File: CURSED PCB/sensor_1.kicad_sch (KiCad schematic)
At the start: 9 parts, among them U1 OPA196xDBV

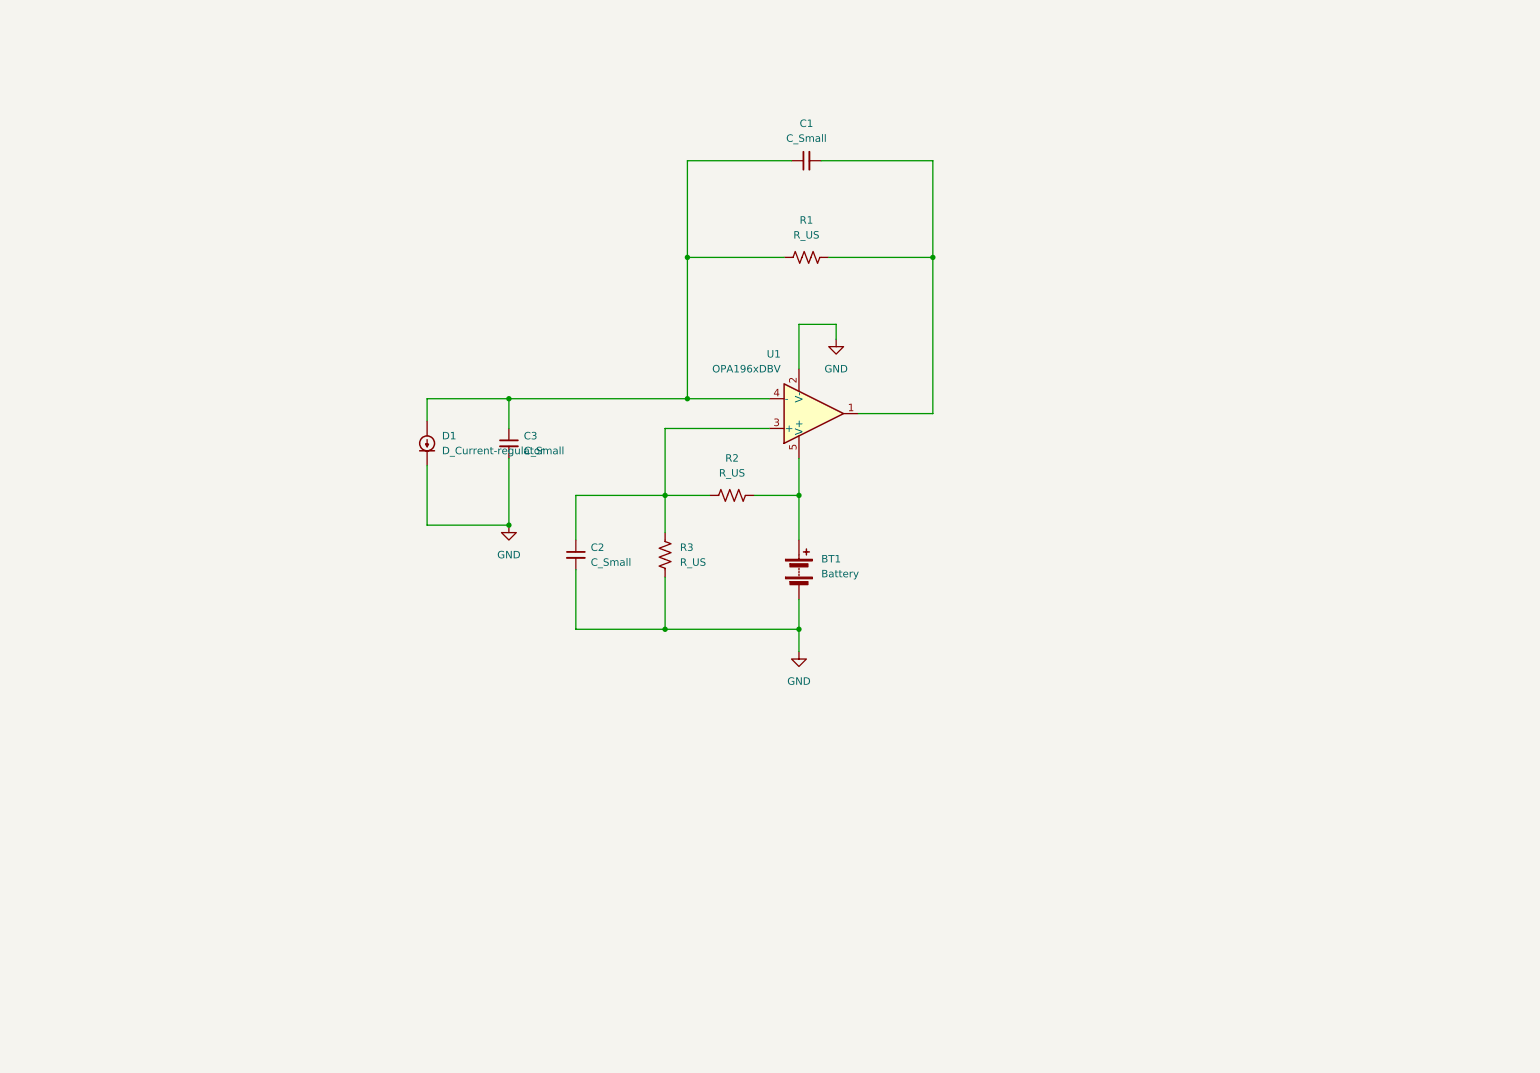
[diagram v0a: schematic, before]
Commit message: Updated PCB compoments
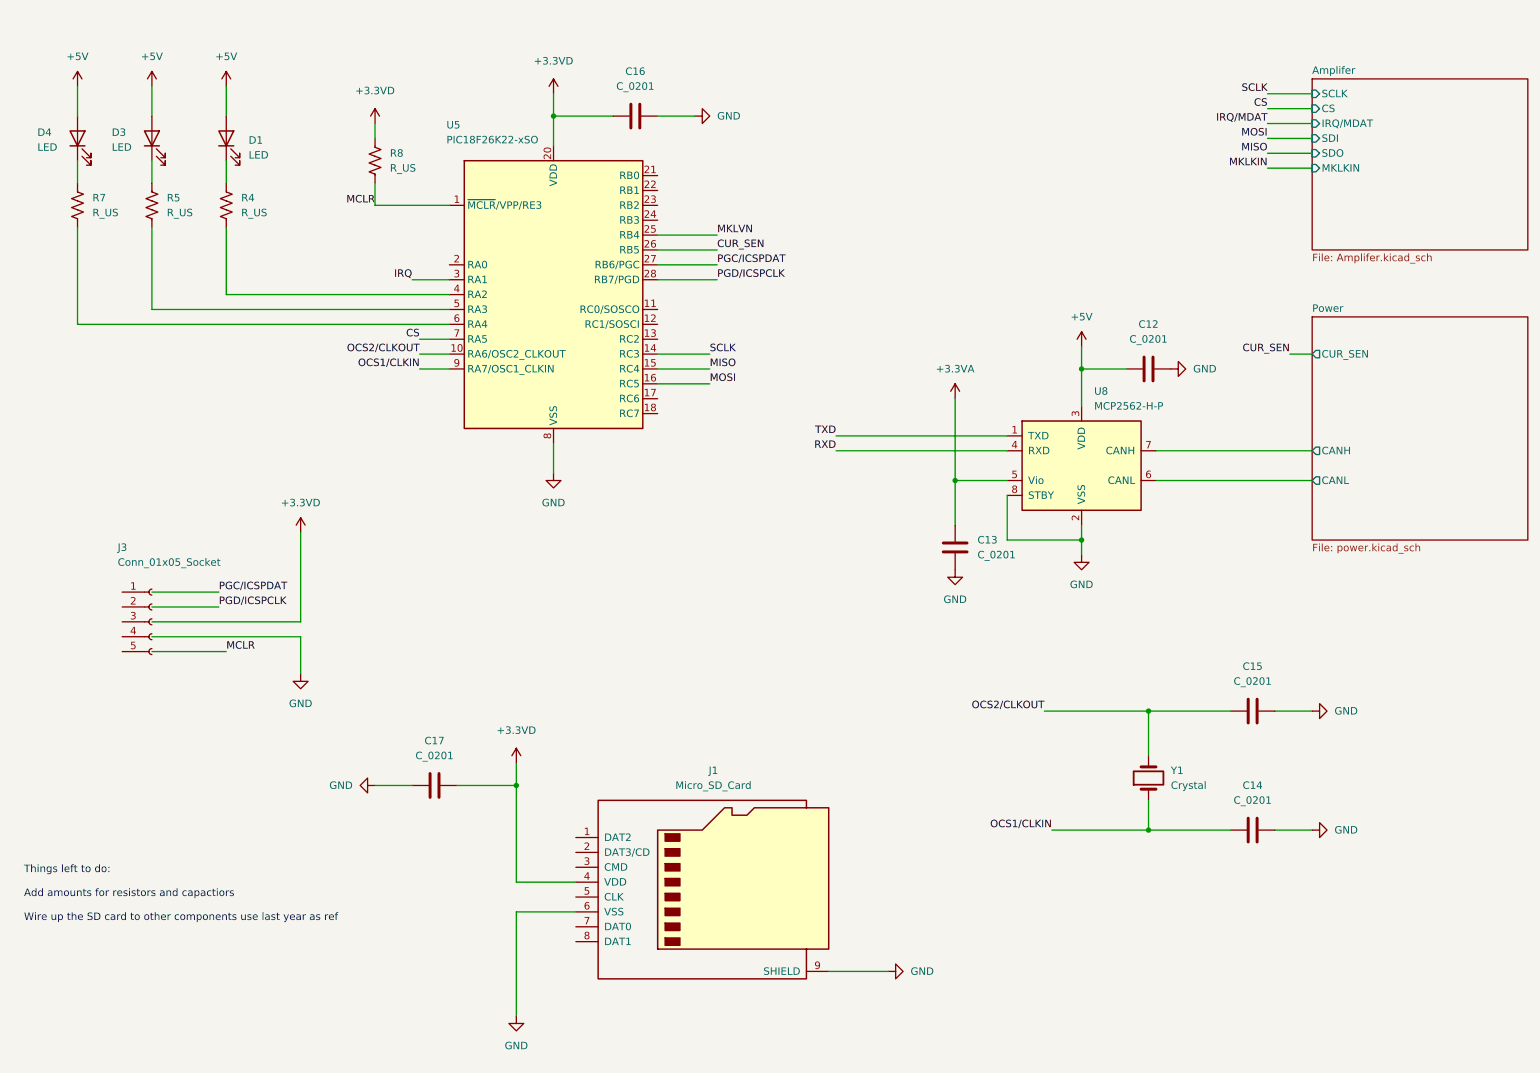
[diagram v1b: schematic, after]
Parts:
- removed BT1: Battery, symbol Device:Battery
- removed C1, C2, C3: C_Small, symbol Device:C_Small
- removed D1: D_Current-regulator, symbol Device:D_Current-regulator
- removed R1, R2, R3: R_US, symbol Device:R_US
- removed U1: OPA196xDBV, Package_TO_SOT_SMD:SOT-23-5, symbol Amplifier_Operational:OPA196xDBV
- added C12, C13, C14, C15, C16, C17: C_0201, PCM_Capacitor_SMD_AKL:C_0201_0603Metric, symbol PCM_Capacitor_US_AKL:C_0201
- added D1, D3, D4: LED, symbol Device:LED
- added J1: Micro_SD_Card, symbol Connector:Micro_SD_Card
- added J3: Conn_01x05_Socket, symbol Connector:Conn_01x05_Socket
- added R4, R5, R7, R8: R_US, symbol Device:R_US
- added U5: PIC18F26K22-xSO, Package_SO:SOIC-28W_7.5x17.9mm_P1.27mm, symbol MCU_Microchip_PIC18:PIC18F26K22-xSO
- added U8: MCP2562-H-P, Package_DIP:DIP-8_W7.62mm, symbol Interface_CAN_LIN:MCP2562-H-P
- added Y1: Crystal, symbol Device:Crystal
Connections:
- net GND: now also C12.2, C13.1, C14.2, C15.2, C16.2, C17.2, J1.6 (VSS), J1.9 (SHIELD), U5.19 (VSS), U5.8 (VSS), U8.2 (VSS), U8.8 (STBY)
- new net: R4.2, U5.4 (RA2)
- new net: R5.2, U5.5 (RA3)
- new net: R7.2, U5.6 (RA4)
- new net: D1.1 (K), R4.1
- new net: D4.1 (K), R7.1
- new net: D3.1 (K), R5.1
- new net +3.3VA: C13.2, U8.5 (Vio)
- new net +3.3VD: C16.1, C17.1, J1.4 (VDD), R8.1, U5.20 (VDD)
- new net +5V: C12.1, D1.2 (A), D3.2 (A), D4.2 (A), U8.3 (VDD)
- new net CS: U5.7 (RA5)
- new net CUR_SEN: U5.26 (RB5)
- new net IRQ: U5.3 (RA1)
- new net MCLR: R8.2, U5.1 (~{MCLR}/VPP/RE3)
- new net MISO: U5.15 (RC4)
- new net MKLVN: U5.25 (RB4)
- new net MOSI: U5.16 (RC5)
- new net OCS1/CLKIN: C14.1, U5.9 (RA7/OSC1_CLKIN), Y1.1
- new net OCS2/CLKOUT: C15.1, U5.10 (RA6/OSC2_CLKOUT), Y1.2
- new net PGC/ICSPDAT: U5.27 (RB6/PGC)
- new net PGD/ICSPCLK: U5.28 (RB7/PGD)
- new net Power/CANH: U8.7 (CANH)
- new net Power/CANL: U8.6 (CANL)
- new net RXD: U8.4 (RXD)
- new net SCLK: U5.14 (RC3)
- new net TXD: U8.1 (TXD)
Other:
- added sheet Amplifer (Amplifer.kicad_sch)
- added sheet Power (power.kicad_sch)
- note added: "Things left to do: Add amounts for resistors and capactiors Wire up the SD card to other components use last year as ref"

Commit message: Added some amplifer stuff
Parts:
- D1: value LED -> RED LED
- D2: renamed from D3; value LED -> BLUE LED
- D3: renamed from D4; value LED -> GREEN LED
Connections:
- net CS: now also J1.2 (DAT3/CD)
- net MISO: now also J1.7 (DAT0)
- net MOSI: now also J1.3 (CMD)
- net SCLK: now also J1.5 (CLK)
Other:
- note added: "Things left to do: Add amounts for resistors and capactiors, use last year as ref"
- note removed: "Things left to do: Add amounts for resistors and capactiors Wire up the SD card to other components use last year as ref"
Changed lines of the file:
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@@
 	(generator_version "9.0")
 	(paper "A4")
-	(text "Things left to do:\n\nAdd amounts for resistors and capactiors\n\nWire up the SD card to other components use last year as ref"
+	(text "Things left to do:\n\nAdd amounts for resistors and capactiors, use last year as ref\n"
 		(exclude_from_sim no)
-		(at 16.256 163.322 0)
+		(at 183.388 174.498 0)
 		(effects
 			(font
@@
 	(wire
 		(pts
+			(xy 63.5 163.83) (xy 110.49 163.83)
+		)
+		(stroke
+			(width 0)
+			(type default)
+		)
+	)
+	(wire
+		(pts
 			(xy 110.49 161.29) (xy 100.33 161.29)
 		)
@@
 	(wire
 		(pts
+			(xy 63.5 168.91) (xy 110.49 168.91)
+		)
+		(stroke
+			(width 0)
+			(type default)
+		)
+	)
+	(wire
+		(pts
 			(xy 196.85 100.33) (xy 196.85 102.87)
 		)
@@
 	(wire
 		(pts
+			(xy 64.77 156.21) (xy 110.49 156.21)
+		)
+		(stroke
+			(width 0)
+			(type default)
+		)
+	)
+	(wire
+		(pts
 			(xy 50.8 60.96) (xy 88.9 60.96)
 		)
@@
 		(pts
 			(xy 38.1 111.76) (xy 49.53 111.76)
+		)
+		(stroke
+			(width 0)
+			(type default)
+		)
+	)
+	(wire
+		(pts
+			(xy 64.77 158.75) (xy 110.49 158.75)
 		)
 		(stroke
@@
 		)
 	)
+	(label "SCLK"
+		(at 63.5 163.83 0)
+		(effects
+			(font
+				(size 1.27 1.27)
+			)
+			(justify left bottom)
+		)
+	)
 	(label "MCLR"
 		(at 76.2 45.72 180)
@@
 		)
 	)
+	(label "MISO"
+		(at 63.5 168.91 0)
+		(effects
+			(font
+				(size 1.27 1.27)
+			)
+			(justify left bottom)
+		)
+	)
 	(label "CS"
 		(at 83.82 68.58 180)
@@
 		)
 	)
+	(label "CS"
+		(at 64.77 156.21 0)
+		(effects
+			(font
+				(size 1.27 1.27)
+			)
+			(justify left bottom)
+		)
+	)
 	(label "OCS2{slash}CLKOUT"
 		(at 190.5 132.08 180)
@@
 			)
 			(justify right bottom)
+		)
+	)
+	(label "MOSI"
+		(at 64.77 158.75 0)
+		(effects
+			(font
+				(size 1.27 1.27)
+			)
+			(justify left bottom)
 		)
 	)
@@
 		(on_board yes)
 		(dnp no)
-		(fields_autoplaced yes)
 		(property "Reference" "D1"
-			(at 54.61 34.6074 90)
+			(at 53.34 27.94 90)
 			(effects
 				(font
@@
 			)
 		)
-		(property "Value" "LED"
-			(at 54.61 37.1474 90)
+		(property "Value" "RED LED"
+			(at 53.34 30.48 90)
 			(effects
 				(font
@@
 		(on_board yes)
 		(dnp no)
-		(property "Reference" "D4"
-			(at 18.542 33.274 90)
+		(property "Reference" "D3"
+			(at 26.67 27.432 90)
 			(effects
 				(font
@@
 			)
 		)
-		(property "Value" "LED"
-			(at 18.542 35.814 90)
+		(property "Value" "GREEN LED"
+			(at 26.67 29.972 90)
 			(effects
 				(font
@@
 			(project "sensor_1"
 				(path "/9fb1a86f-679c-4b88-9ed1-932f4f414580"
-					(reference "D4")
+					(reference "D3")
 					(unit 1)
 				)
@@
 		(on_board yes)
 		(dnp no)
-		(property "Reference" "D3"
-			(at 31.242 33.274 90)
+		(property "Reference" "D2"
+			(at 40.132 28.194 90)
 			(effects
 				(font
@@
 			)
 		)
-		(property "Value" "LED"
-			(at 31.242 35.814 90)
+		(property "Value" "BLUE LED"
+			(at 40.132 30.734 90)
 			(effects
 				(font
@@
 			(project "sensor_1"
 				(path "/9fb1a86f-679c-4b88-9ed1-932f4f414580"
-					(reference "D3")
+					(reference "D2")
 					(unit 1)
 				)

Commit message: Updates to PCB before exam sesaon
idk what I added ngl
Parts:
- C16: value C_0201 -> 0.1µF
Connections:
- net TXD/CANTX: now reaches U5.11 (RC0/SOSCO)
- net RXD/CANRX: now reaches U5.12 (RC1/SOSCI)
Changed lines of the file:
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@@
+	(wire
+		(pts
+			(xy 124.46 66.04) (xy 134.62 66.04)
+		)
+		(stroke
+			(width 0)
+			(type default)
+		)
+	)
 	(wire
 		(pts
@@
 		(pts
 			(xy 196.85 73.66) (xy 204.47 73.66)
+		)
+		(stroke
+			(width 0)
+			(type default)
+		)
+	)
+	(wire
+		(pts
+			(xy 124.46 63.5) (xy 134.62 63.5)
 		)
 		(stroke
@@
 		)
 	)
+	(label "TXD{slash}CANTX"
+		(at 134.62 63.5 0)
+		(effects
+			(font
+				(size 1.27 1.27)
+			)
+			(justify left bottom)
+		)
+	)
 	(label "PGC{slash}ICSPDAT"
 		(at 49.53 111.76 0)
@@
 			)
 			(justify right bottom)
+		)
+	)
+	(label "RXD{slash}CANRX"
+		(at 134.62 66.04 0)
+		(effects
+			(font
+				(size 1.27 1.27)
+			)
+			(justify left bottom)
 		)
 	)
@@
 			)
 		)
-		(property "Value" "C_0201"
+		(property "Value" "0.1µF"
 			(at 120.65 25.4 90)
 			(effects

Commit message: Added values for schematic
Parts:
- C12, C13, C17: value C_0201 -> 0.1uF
- C14, C15: value C_0201 -> 27pF
- R4, R7: value R_US -> 500R
- R5: value R_US -> 330R
- R8: value R_US -> 10k
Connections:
- net +3.3VD: now also J3.3 (Pin_3)
- net GND: now also J3.4 (Pin_4)
- net MCLR: now also J3.5 (Pin_5)
- net PGC/ICSPDAT: now also J3.1 (Pin_1)
- net PGD/ICSPCLK: now also J3.2 (Pin_2)
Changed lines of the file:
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@@
 	(wire
 		(pts
-			(xy 38.1 116.84) (xy 63.5 116.84)
+			(xy 38.1 119.38) (xy 63.5 119.38)
 		)
 		(stroke
@@
 	(wire
 		(pts
+			(xy 38.1 121.92) (xy 50.8 121.92)
+		)
+		(stroke
+			(width 0)
+			(type default)
+		)
+	)
+	(wire
+		(pts
 			(xy 83.82 71.12) (xy 88.9 71.12)
 		)
@@
 	(wire
 		(pts
-			(xy 38.1 121.92) (xy 50.8 121.92)
+			(xy 124.46 71.12) (xy 133.35 71.12)
 		)
 		(stroke
@@
 	(wire
 		(pts
-			(xy 124.46 71.12) (xy 133.35 71.12)
+			(xy 208.28 147.32) (xy 208.28 152.4)
 		)
 		(stroke
@@
 	(wire
 		(pts
-			(xy 208.28 147.32) (xy 208.28 152.4)
+			(xy 38.1 38.1) (xy 38.1 41.91)
 		)
 		(stroke
@@
 	(wire
 		(pts
-			(xy 38.1 38.1) (xy 38.1 41.91)
+			(xy 228.6 31.75) (xy 236.22 31.75)
 		)
 		(stroke
@@
 	(wire
 		(pts
-			(xy 228.6 31.75) (xy 236.22 31.75)
+			(xy 38.1 116.84) (xy 63.5 116.84)
 		)
 		(stroke
@@
 	(wire
 		(pts
-			(xy 38.1 119.38) (xy 63.5 119.38)
-		)
-		(stroke
-			(width 0)
-			(type default)
-		)
-	)
-	(wire
-		(pts
 			(xy 82.55 144.78) (xy 76.2 144.78)
 		)
@@
 	(wire
 		(pts
-			(xy 38.1 111.76) (xy 49.53 111.76)
+			(xy 64.77 158.75) (xy 110.49 158.75)
 		)
 		(stroke
@@
 	(wire
 		(pts
-			(xy 64.77 158.75) (xy 110.49 158.75)
+			(xy 196.85 73.66) (xy 204.47 73.66)
 		)
 		(stroke
@@
 	(wire
 		(pts
-			(xy 196.85 73.66) (xy 204.47 73.66)
+			(xy 124.46 63.5) (xy 134.62 63.5)
 		)
 		(stroke
@@
 	(wire
 		(pts
-			(xy 124.46 63.5) (xy 134.62 63.5)
+			(xy 38.1 111.76) (xy 49.53 111.76)
 		)
 		(stroke
@@
 			)
 		)
-		(property "Value" "C_0201"
+		(property "Value" "27pF"
 			(at 226.06 127 90)
 			(effects
@@
 			)
 		)
-		(property "Value" "C_0201"
+		(property "Value" "0.1uF"
 			(at 208.28 68.58 90)
 			(effects
@@
 			)
 		)
-		(property "Value" "R_US"
+		(property "Value" "330R"
 			(at 40.64 46.9899 0)
 			(effects
@@
 			)
 		)
-		(property "Value" "C_0201"
+		(property "Value" "0.1uF"
 			(at 179.07 105.4099 0)
 			(effects
@@
 			)
 		)
-		(property "Value" "C_0201"
+		(property "Value" "27pF"
 			(at 226.06 147.32 90)
 			(effects
@@
 			)
 		)
-		(property "Value" "C_0201"
+		(property "Value" "0.1uF"
 			(at 86.36 139.7 90)
 			(effects
@@
 	(symbol
 		(lib_id "Connector:Conn_01x05_Socket")
-		(at 38.1 116.84 0)
+		(at 33.02 116.84 0)
+		(mirror y)
 		(unit 1)
 		(exclude_from_sim no)
@@
 		(dnp no)
 		(property "Reference" "J3"
-			(at 32.258 104.14 0)
+			(at 38.862 104.14 0)
 			(effects
 				(font
@@
 		)
 		(property "Value" "Conn_01x05_Socket"
-			(at 32.258 106.68 0)
+			(at 38.862 106.68 0)
 			(effects
 				(font
@@
 		)
 		(property "Footprint" ""
-			(at 38.1 116.84 0)
+			(at 33.02 116.84 0)
 			(effects
 				(font
@@
 		)
 		(property "Datasheet" "~"
-			(at 38.1 116.84 0)
+			(at 33.02 116.84 0)
 			(effects
 				(font
@@
 		)
 		(property "Description" "Generic connector, single row, 01x05, script generated"
-			(at 38.1 116.84 0)
+			(at 33.02 116.84 0)
 			(effects
 				(font
@@
 			)
 		)
-		(property "Value" "R_US"
+		(property "Value" "500R"
 			(at 53.34 46.9899 0)
 			(effects
@@
 			)
 		)
-		(property "Value" "R_US"
+		(property "Value" "500R"
 			(at 27.94 46.9899 0)
 			(effects
@@
 			)
 		)
-		(property "Value" "R_US"
+		(property "Value" "10k"
 			(at 78.74 39.3699 0)
 			(effects
